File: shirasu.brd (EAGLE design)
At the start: 100 x 50 mm, 122 parts, among them J1 XT60PW-F, J2 XT60PW-M, J3 EP2.5-4-SIDE, J4 EP2.5-4-SIDE, J5 RJHSE-5381-02, J6 10118192-0001LF, Q1 TPH1R405PL,L1Q, Q2 TPH1R405PL,L1Q, Q3 TPH1R405PL,L1Q, Q4 TPH1R405PL,L1Q, U1 STM32F302_303C2, U10 MC34063AD, U11 INA2181A1IDGSR, U12 CSTNE_GH5L, U2 NCV7351D1E, U3 SI8621EC-B-IS, U4 TLP291, U5 BSS138BK, U6 MIC4606-2YTS-TR, U7 7812DT, U8 7805DT, U9 XC6206

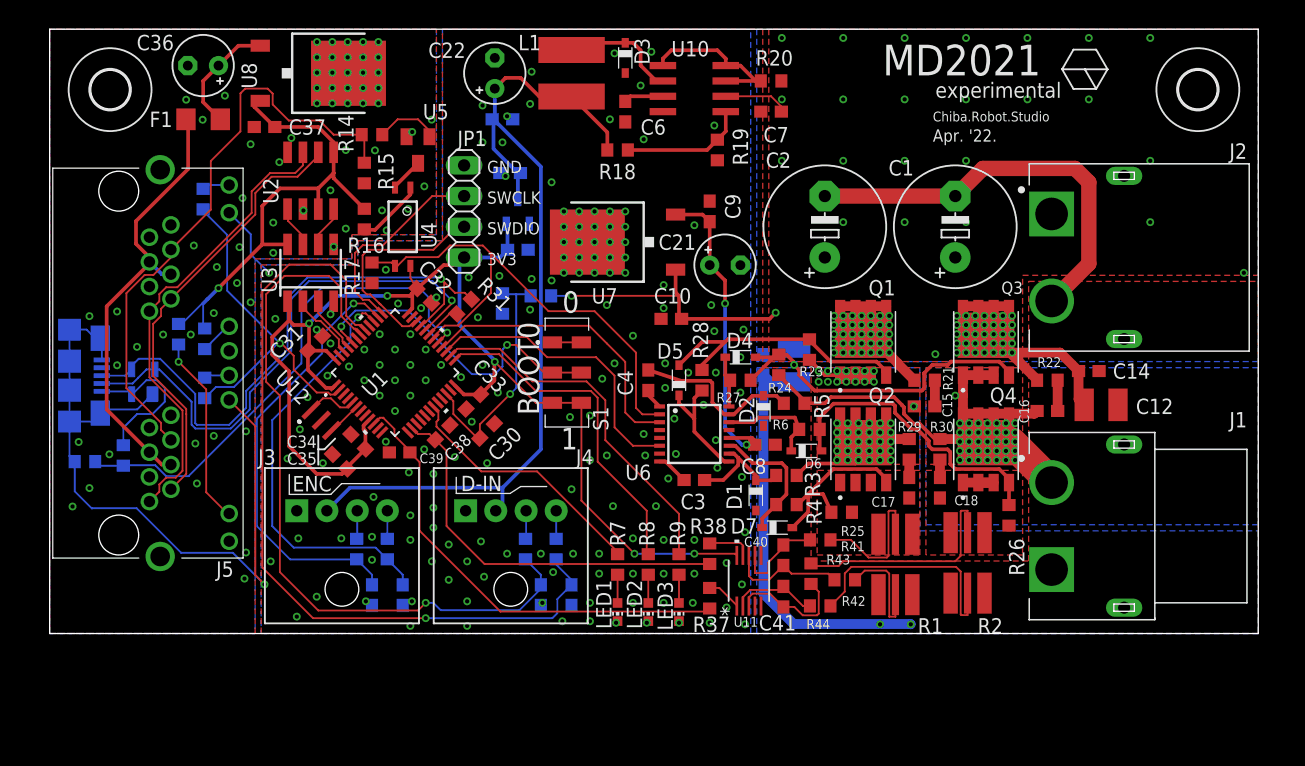
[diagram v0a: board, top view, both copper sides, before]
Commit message: fixed xt connector removed some resistors and capacitors
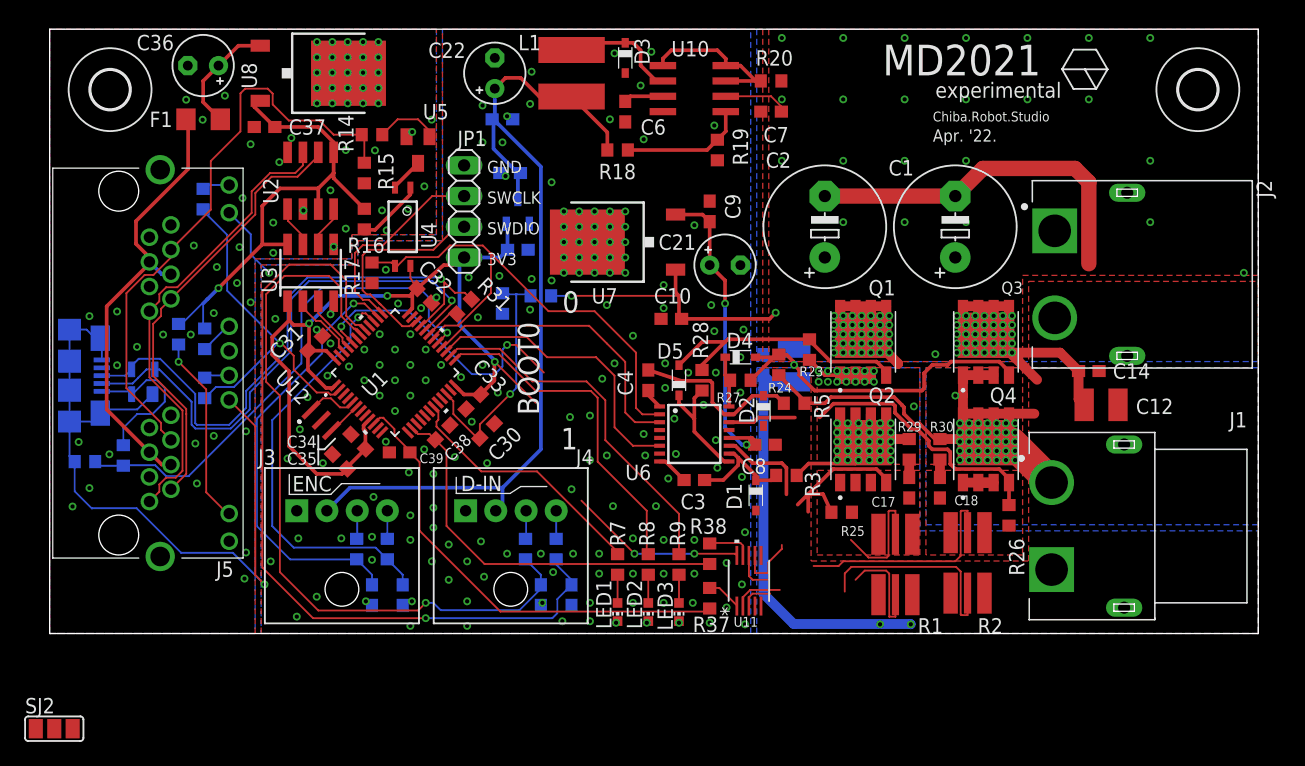
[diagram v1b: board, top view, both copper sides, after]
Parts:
- removed C15, C16, C40, C41: (no value), rcl:C0603
- removed D6, D7: PMEG6010CEJ,115, nexperia:SOD323_ST
- removed R21, R22, R4, R41, R42, R43, R44, R6: (no value), rcl:R0603
- removed S1: JS202011JCQN, switch-slide:JS202011JCQN
- added SJ2: (no value), jumper:SJ_2
- moved J2 1.42 mm to (89.2, 29.7)
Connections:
- removed net N$29: C15.2, R21.1
- removed net N$31: C16.2, R22.1
- removed net N$45: C40.2, R41.1, U11.7
- removed net N$46: C40.1, R42.1, U11.8
- removed net N$53: C41.1, R44.2, U11.2
- removed net N$54: C41.2, R43.2, U11.3
- removed net N$6: D6.C, R6.1, U6.14
- removed net N$7: D7.C, R4.1, U6.11
- net +3V3: now also SJ2.1; no longer S1.3, S1.5
- net ALG: now also U6.11; no longer D7.A, R4.2
- net BLG: now also U6.14; no longer D6.A, R6.2
- net GNDA: now also J2.1, SJ2.3; no longer J2.2, S1.1, S1.7
- net N$48: now also U11.7; no longer R41.2
- net N$49: now also SJ2.2; no longer S1.2, S1.6
- net N$50: now also U11.8; no longer R42.2
- net N$51: now also U11.3; no longer R43.1
- net N$52: now also U11.2; no longer R44.1
- net OUT+: no longer C15.1
- net OUT-: no longer C16.1
- net VCC: now also J2.2; no longer J2.1, R21.2, R22.2
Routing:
- net +3V3: track 107.3 -> 95.4 mm
- net N$7: track 11.3 -> 0.00 mm
- net N$54: track 10.2 -> 0.00 mm
- net N$46: track 9.90 -> 0.00 mm
- net N$6: track 8.70 -> 0.00 mm
- net N$45: track 7.85 -> 0.00 mm
- net N$53: track 7.32 -> 0.00 mm
- net GNDA: track 139.4 -> 132.7 mm
- net ALG: track 15.5 -> 21.2 mm
- net N$48: track 11.7 -> 15.3 mm
- net N$50: track 9.14 -> 12.6 mm
- net N$49: track 27.2 -> 24.1 mm
- net BLG: track 24.9 -> 27.7 mm
- net N$31: track 2.54 -> 0.00 mm
- net N$52: track 19.1 -> 21.5 mm
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
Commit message: ver1.0
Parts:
- removed C13, C14, C24, C25, C26, C27: (no value), rcl:C0603
- removed C36: (no value), rcl:E2,5-5
- removed R13, R14, R17, R20, R23, R24, R25, R26, R33, R34, R35, R36: (no value), rcl:R0603
- removed R32: 4k7, rcl:R0603
- removed R45: 10k, rcl:R0603
- removed U6: MIC4606-2YTS-TR, Microchip:TSSOP16
- removed U7: 7812DT, linear:TO252
- removed U8: 7805DT, linear:TO252
- added C15: 2.2u, rcl:C0603
- added C16, C23: 100n, rcl:C0603
- added IC1: 78L12F, linear:SOT89
- added IC2: 78L05F, linear:SOT89
- added R4: 100, rcl:R0603
- added R6: 180, rcl:R0603
- added RT1: NCP15XH103F03RC, NCP15XH103F03RC:THRMC1005X55N
- added U$1: MIC4606-2YTS-TR, Microchip:TSSOP16
- C10, C30, C31, C32, C33, C5, C7: value (none) -> 100n
- C17, C18: value (none) -> 470n
- C19, C20, C38, C39, C8: value (none) -> 1u
- C21: value (none) -> 100n; device rcl:E2,5-5 -> rcl:C0603
- C34: value 100n -> 10n
- C37, C9: value (none) -> 330n
- C6: value (none) -> 470p
- R10: value 4k7 -> 3.3k
- R11: value 4k7 -> 0.68; device rcl:R0603 -> rcl:R1206
- R12: value (none) -> 180
- R15, R39: value (none) -> 10k
- R16: value (none) -> 470
- R18: value (none) -> 3.6k
- R19, R7, R8, R9: value (none) -> 1.2k
- R27, R28: value (none) -> 40
- R29, R30: value (none) -> 2
- R3, R5: value (none) -> 3
- R37, R38: value (none) -> 10
- R40: value (none) -> 1k
- moved SJ2 92.1 mm to (83.7, 31.3), flipped to the bottom, turned to 225 degrees
- moved J6 91.0 mm to (95.3, 25.1), turned to 270 degrees
- moved H1 90.2 mm to (95.2, 45.0)
- moved H2 89.7 mm to (5.33, 45.0)
- moved D8 84.1 mm to (91.7, 25.5), turned to 270 degrees
- moved J5 83.8 mm to (91.8, 20.1), turned to 90 degrees
- moved J2 81.3 mm to (10.6, 8.90), turned to 90 degrees
- moved J1 80.1 mm to (10.6, 25.4), turned to 90 degrees
- moved F1 74.5 mm to (87.2, 42.0)
- moved R12 70.2 mm to (82.8, 31.9), flipped to the top
- moved C37 65.3 mm to (82.9, 46.4), turned to 90 degrees
- moved U3 59.3 mm to (80.4, 37.8), flipped to the bottom
- moved U2 59.3 mm to (80.4, 45.2), flipped to the bottom
- moved R15 59.0 mm to (80.7, 15.8), turned to 180 degrees
- moved C31 57.7 mm to (78.8, 34.0), turned to 135 degrees
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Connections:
- net N$49 renamed BOOT0
- removed net N$18: J5.B10, R11.2
- removed net N$20: J5.A10, R10.2
- removed net N$21: J5.B12, R13.2
- removed net N$37: D8.2, J6.1, R32.2
- removed net N$38: J3.4, R34.1
- removed net N$40: J3.3, R33.1
- removed net N$43: J4.3, R35.1
- removed net N$44: J4.4, R36.1
- removed net N$48: R1.6, U11.7
- removed net N$50: R1.5, U11.8
- removed net N$51: R2.5, U11.3
- removed net N$52: R2.6, U11.2
- new net N$29: R2.6, U11.8
- new net N$31: R1.5, U11.2
- new net N$6: J5.B10, R4.2
- new net N$7: J5.A10, J5.B9
- new net TEMP: C15.2, R10.2, RT1.1, U1.14
- net !EMS: now also U$1.2; no longer R17.2, U6.2
- net +12V: now also IC1.1, U$1.12; no longer C21.+, U6.12, U7.2
- net +3V3: now also C23.1, R31.1, RT1.2
- net 5V_ISO: now also C21.2, IC2.1, R4.1; no longer R10.1, R11.1, U8.2
- net AHG: no longer R23.2
- net ALG: now also U$1.11; no longer R25.1, U6.11
- net APWM: now also U$1.6, U1.12; no longer U1.27, U6.6
- net BHG: no longer R24.1
- net BLG: now also U$1.14; no longer R26.1, U6.14
- net BPWM: now also U$1.3, U1.13; no longer U1.28, U6.3
- net DIN_A: now also J4.3, U1.29; no longer C27.2, R35.2, U1.42
- net DIN_B: now also J4.4, U1.31; no longer C26.2, R36.2, U1.41
- net ENC_A: now also J3.3; no longer C25.2, R33.2
- net ENC_B: now also J3.4; no longer C24.2, R34.2
- net GNDA: now also C15.1, C23.2, IC1.2, IC1.2@1, R10.1, U$1.13, U$1.4, U$1.5, U$1.7; no longer C13.2, C14.2, C21.-, C24.1, C25.1, C26.1, C27.1, R17.1, R45.2, U6.13, U7.3
- net GNDIO: now also C16.2, C21.1, IC2.2, IC2.2@1; no longer C36.-, J5.B9, U8.3
- net ISENSEA: now also U1.17; no longer U1.14
- net ISENSEB: now also U1.11; no longer U1.10
- net LED_CAN: now also R6.2, U1.40; no longer R13.1, U1.2
- net LED_GREEN: now also U1.25; no longer U1.19
- net LED_RED: now also U1.27; no longer U1.26
- net LED_YELLOW: now also U1.26; no longer U1.25
- net N$12: now also J5.A12, R6.1; no longer R31.1, U1.31
- net N$13: now also J5.B12, R12.2; no longer R32.1, R45.1, U1.29
- net N$17: now also U5.1; no longer R14.2
- net N$19: now also C16.1, IC2.3; no longer C36.+, U8.1
- net N$22: now also R1.6, U11.3; no longer J5.A12, R12.2
- net N$23: now also R2.5, U11.7; no longer R14.1, U5.1
- net N$3: now also U$1.10; no longer U6.10
- net N$30: now also R11.2; no longer R20.1
- net N$32: now also U$1.16; no longer U6.16
- net N$33: now also U$1.9; no longer U6.9
- net N$4: now also U$1.8; no longer U6.8
- net N$5: now also U$1.15; no longer U6.15
- net N$8: now also U$1.1; no longer U6.1
- net OUT+: no longer R23.1
- net OUT-: no longer R24.2
- net VCC: now also IC1.3, R11.1; no longer C13.1, C14.1, R20.2, U7.1
- net VCSA: no longer R25.2
- net VCSB: no longer R26.2
- net VSENSE: now also U1.10; no longer U1.22
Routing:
- net GNDIO: track 0.00 -> 124.4 mm, vias 68 -> 3
- net GNDA: track 132.7 -> 22.7 mm, vias 170 -> 66
- net DIN_B: track 68.0 -> 24.2 mm, vias 1 -> 0
- net DIN_A: track 62.4 -> 23.6 mm, vias 1 -> 0
- net +3V3: track 95.4 -> 131.0 mm, vias 5 -> 7
- net OUT-: track 42.1 -> 7.49 mm, vias 36 -> 26
- net TEMP: track 0.00 -> 33.5 mm, vias 0 -> 1
- net N$13: track 42.6 -> 9.16 mm, vias 1 -> 0
- net ISENSEB: track 38.5 -> 5.38 mm, vias 0 -> 1
- net 5V_ISO: track 41.4 -> 72.7 mm, vias 1 -> 2
- net USB_DP: track 49.0 -> 22.1 mm
- net ISENSEA: track 32.9 -> 6.79 mm
- net N$32: track 4.28 -> 29.2 mm, vias 0 -> 2
- net USB_DM: track 45.0 -> 20.9 mm
- net BHG: track 27.7 -> 4.42 mm, vias 1 -> 0
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- removed copper zone on layer 1, net GNDIO
- removed copper zone on layer 16, net GNDIO
- removed copper zone on layer 16, net VCC
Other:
- board text added: "C:/Users/ryuni/Desktop/python_workspace/image_th.bmp"
- board text added: "ver1.0"
- board text removed: "0"
- board text removed: "1"
- board text removed: "3V3"
- board text removed: "Apr. '22."
- board text removed: "BOOT0"
- board text removed: "Chiba.Robot.Studio"
- board text removed: "D-IN"
- board text removed: "ENC"
- board text removed: "MD2021"
- board text removed: "SWCLK"
- board text removed: "SWDIO"
- board text removed: "experimental"

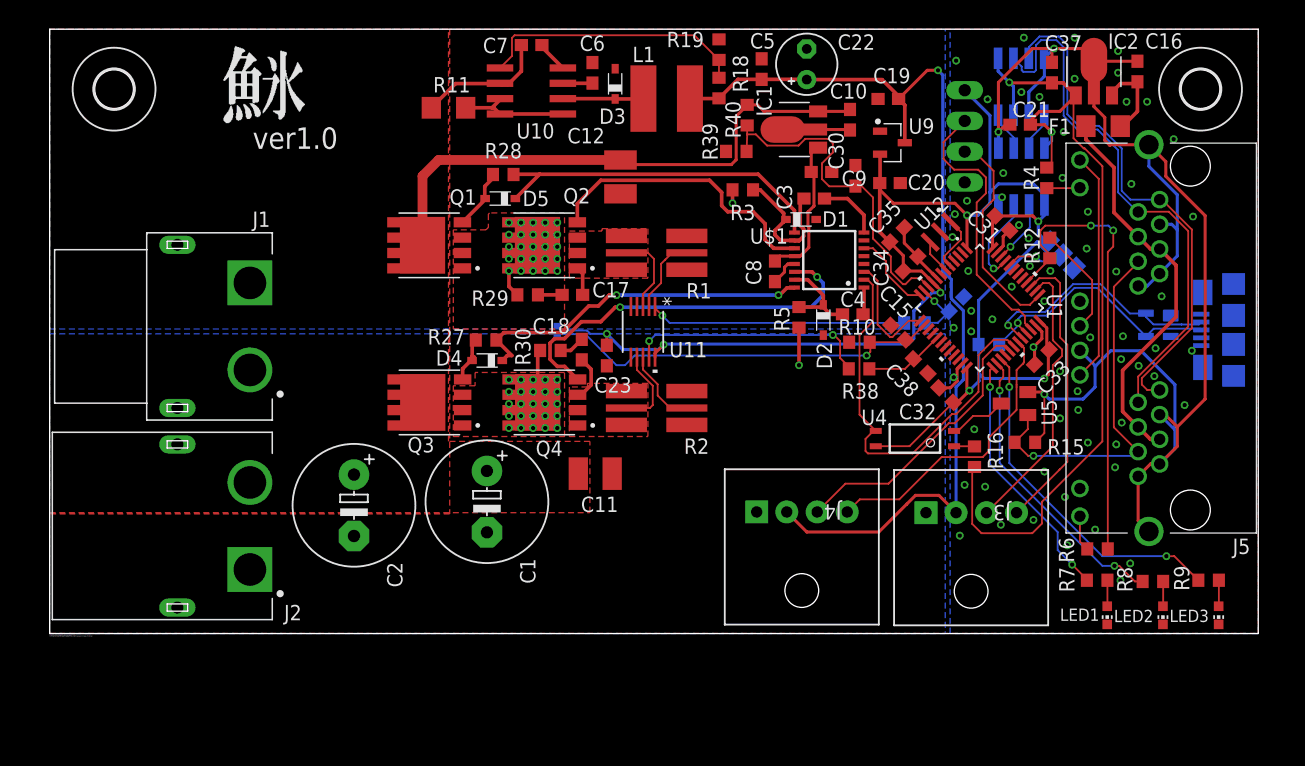
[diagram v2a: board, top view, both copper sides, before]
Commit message: use TIM1 for pwm instead of TIM15,add gate resistors for low side MOSFET as well.
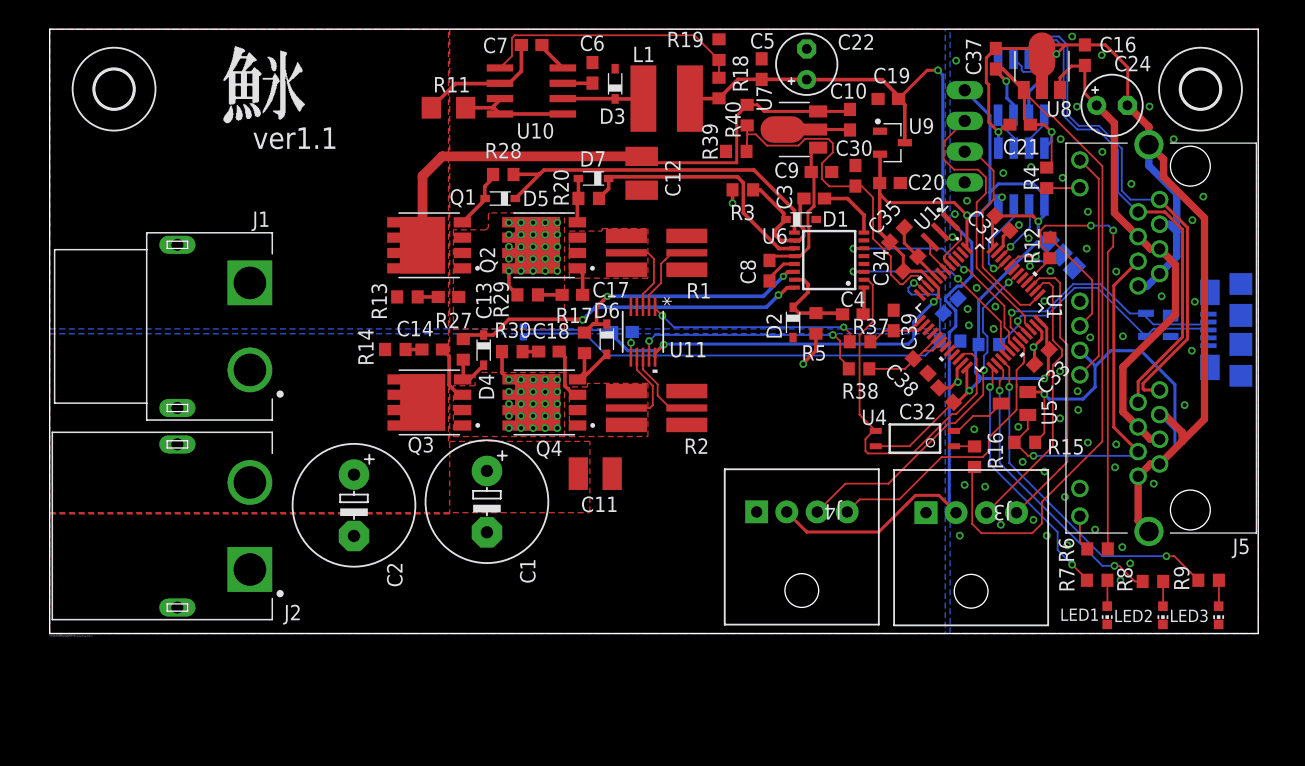
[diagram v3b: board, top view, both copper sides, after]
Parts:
- removed F1: (no value), rcl:R1206
- removed IC2: 78L05F, linear:SOT89
- added C13, C14: 6800p, rcl:C0603
- added C24: (no value), rcl:E2,5-5
- added D6, D7: PMEG6010CEJ,115, nexperia:SOD323_ST
- added R13, R14, R17, R20: 2, rcl:R0603
- added U8: 78L05F, linear:SOT89
- C17, C18: value 470n -> 6800p
- R27: value 40 -> 2
- moved R10 7.50 mm to (74.5, 24.2), flipped to the bottom
- moved C39 5.37 mm to (69.8, 25.9), flipped to the top, turned to 270 degrees
- moved C15 4.87 mm to (74.5, 27.1), flipped to the bottom
- moved C37 4.79 mm to (78.3, 47.6)
- moved R37 4.77 mm to (67.0, 24.1), flipped to the top, turned to 0 degrees
- moved C16 4.55 mm to (85.7, 47.9)
- moved R30 3.15 mm to (38.3, 23.3)
- moved RT1 2.80 mm to (39.2, 24.9)
- moved C18 2.72 mm to (41.3, 23.3), turned to 180 degrees
- moved D2 2.51 mm to (61.5, 25.7)
- moved C23 2.32 mm to (47.4, 24.9), flipped to the bottom, turned to 180 degrees
- moved R27 2.04 mm to (34.2, 23.5), turned to 90 degrees
- moved C12 1.78 mm to (49.0, 38.1)
- moved R5 1.49 mm to (63.4, 25.7)
- moved D4 0.91 mm to (35.9, 23.4), turned to 270 degrees
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- renumbered IC1 to U7, SJ2 to BOOT0, U$1 to U6
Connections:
- new net N$18: C14.2, R14.1
- new net N$20: C13.2, R13.1
- new net N$21: D7.C, R20.1, U6.11
- net !EMS: now also U1.22; no longer U1.30
- net 5V_ISO: now also U8.1; no longer IC2.1
- net ALG: now also D7.A, R20.2; no longer U6.11
- net APWM: now also U1.30; no longer U1.12
- net BLG: now also D6.A, R17.2; no longer U6.14
- net BPWM: now also U1.29; no longer U1.13
- net DIN_A: now also U1.42; no longer U1.29
- net GNDIO: now also C24.-, U8.2, U8.2@1; no longer IC2.2, IC2.2@1
- net ISENSEA: now also U1.18
- net ISENSEB: now also U1.13, U1.14; no longer U1.11
- net N$15: now also C16.1, C24.+, U8.3; no longer F1.2
- net N$19: now also D6.C, R17.1, U6.14; no longer C16.1, F1.1, IC2.3
- net OUT+: now also C13.1
- net OUT-: now also C14.1
- net TEMP: now also U1.11; no longer U1.14
- net VCC: now also R13.2, R14.2
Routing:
- net BLG: track 32.3 -> 5.62 mm, vias 2 -> 0
- net N$21: track 0.00 -> 21.3 mm
- net ALG: track 24.1 -> 3.66 mm
- net N$19: track 7.11 -> 21.1 mm, vias 0 -> 2
- net APWM: track 6.82 -> 19.0 mm, vias 0 -> 2
- net TEMP: track 33.5 -> 44.5 mm
- net N$15: track 33.0 -> 41.5 mm
- net BPWM: track 9.54 -> 17.5 mm, vias 0 -> 2
- net DIN_A: track 23.6 -> 29.3 mm, vias 0 -> 2
- net OPOUTB: track 21.3 -> 17.8 mm, vias 1 -> 2
- net GNDIO: track 124.4 -> 127.5 mm
- net OUT-: track 7.49 -> 10.1 mm
- net GNDA: track 22.7 -> 25.1 mm, vias 66 -> 64
- net !EMS: track 34.4 -> 32.2 mm
- net +5V: track 81.0 -> 83.0 mm
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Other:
- board text added: "0"
- board text added: "1"
- board text added: "3V3"
- board text added: "SWCLK"
- board text added: "SWDIO"
- board text added: "ver1.1"
- board text removed: "ver1.0"

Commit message: BOMを追加
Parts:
- C1, C2: value (none) -> 220u
- C15: value 2.2u -> 1u
- C22, C24: value (none) -> 47u
- C38, C39: value 1u -> 330p
- C6: value 470p -> 100p
- LED1: value (none) -> RED
- LED2: value (none) -> YELLOW
- LED3: value (none) -> GREEN
- R1, R2: value (none) -> 1m
- R28: value 40 -> 2
- R3, R5: value 3 -> 2
- R37, R38: value 10 -> 1k
